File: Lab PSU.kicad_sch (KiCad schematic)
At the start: 2 parts, among them T1 Transformer_1P_SS, T2 Transformer_1P_SS

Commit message: many changes
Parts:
- removed T1, T2: Transformer_1P_SS, symbol Device:Transformer_1P_SS
- added C1, C2, C3, C4: 2200u, Capacitor_THT:CP_Radial_D18.0mm_P7.50mm, symbol Device:C_Polarized
- added C27, C28, C35: 10u, Capacitor_THT:CP_Radial_D18.0mm_P7.50mm, symbol Device:C_Polarized
- added C29, C33, C34: 220u, Capacitor_THT:CP_Radial_D18.0mm_P7.50mm, symbol Device:C_Polarized
- added C31, C32, C37: 22u, Capacitor_THT:CP_Radial_D18.0mm_P7.50mm, symbol Device:C_Polarized
- added C36, C38, C39: 100n, Capacitor_SMD:C_1210_3225Metric_Pad1.33x2.70mm_HandSolder, symbol Device:C
- added D1, D10, D11, D12, D13, D14, D15, D16, D2, D24, D25, D26, D27, D28, D29, D3, D30, D31, D4, D5, D6, D7, D8, D9: 1N5406, Diode_THT:D_DO-201AD_P15.24mm_Horizontal, symbol Diode:1N5406
- added F1: 3A slow, symbol Device:Fuse
- added F2, F3: 1A slow, symbol Device:Fuse
- added J1: Screw_Terminal_01x04, TerminalBlock_4Ucon:TerminalBlock_4Ucon_1x04_P3.50mm_Vertical, symbol Connector:Screw_Terminal_01x04
- added J4, J5, J6, J7: Screw_Terminal_01x03, TerminalBlock_4Ucon:TerminalBlock_4Ucon_1x03_P3.50mm_Vertical, symbol Connector:Screw_Terminal_01x03
- added R47, R48, R55: 120, Resistor_SMD:R_1210_3225Metric_Pad1.30x2.65mm_HandSolder, symbol Device:R
- added R49, R50, R57: 330, Resistor_SMD:R_1210_3225Metric_Pad1.30x2.65mm_HandSolder, symbol Device:R
- added RV2, RV3, RV8: 2.5k, Potentiometer_THT:Potentiometer_Bourns_3299W_Vertical, symbol Device:R_Potentiometer_Trim
- added SW3: SW_DPDT_x2, symbol Switch:SW_DPDT_x2
- added T1: PowerTran M5225C, symbol Device:Transformer_1P_2S
- added TR1, TR2: PowerTran M4318, Transformers:Transformer 53x53, symbol Transformer:TRANSF6
- added U14, U17: LM317_SOT-223, Package_TO_SOT_SMD:SOT-223-3_TabPin2, symbol Regulator_Linear:LM317_SOT-223
- added U15: LM337_SOT223, Package_TO_SOT_SMD:SOT-223-3_TabPin2, symbol Regulator_Linear:LM337_SOT223
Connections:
- net 230VAC: now also F1.1, F2.1, F3.1, SW3.3 (C)
- net GND: now also C1.2, C2.2, C29.2, C3.2, C35.2, C37.2, C39.1, C4.2, D1.2 (A), D13.2 (A), D14.2 (A), D15.2 (A), D16.2 (A), D2.2 (A), D26.2 (A), D27.2 (A), D28.1 (K), D28.2 (A), D3.2 (A), D4.2 (A), R57.1, RV8.2, RV8.3, TR2.5, TR2.7
- net NEUT: now also J6.2 (Pin_2), J7.2 (Pin_2), SW3.6 (C), T1.2 (AB), TR1.4, TR2.4
- new net: F2.2, J6.1 (Pin_1), TR1.1
- new net: TR1.2, TR1.3
- new net: F3.2, J7.1 (Pin_1), TR2.1
- new net: C34.2, D30.2 (A), D31.2 (A), U15.2 (VI)
- new net: F1.2, T1.1 (AA)
- new net: C27.2, R48.1, RV2.1, U15.1 (ADJ)
- new net: J1.4 (Pin_4), T1.4 (SB)
- new net: J1.1 (Pin_1), T1.5 (SC)
- new net: C35.1, R55.1, RV8.1, U17.1 (ADJ)
- new net: C28.1, R47.2, RV3.1, U14.1 (ADJ)
- new net: C33.1, D24.1 (K), D29.1 (K), U14.3 (VI)
- new net: C29.1, D25.1 (K), D27.1 (K), U17.3 (VI)
- new net: TR2.2, TR2.3
- new net +25VAC: D1.1 (K), D2.1 (K), D3.1 (K), D4.1 (K), D5.2 (A), D6.2 (A), D7.2 (A), D8.2 (A), J1.2 (Pin_2), T1.3 (SA)
- new net +35VDC: C1.1, C2.1, C3.1, C4.1, D10.1 (K), D11.1 (K), D12.1 (K), D5.1 (K), D6.1 (K), D7.1 (K), D8.1 (K), D9.1 (K)
- new net +5V: C37.1, C39.2, R55.2, R57.2, U17.2 (VO)
- new net +9VAC: D25.2 (A), D26.1 (K), TR2.6, TR2.8
- new net 0VAC: D10.2 (A), D11.2 (A), D12.2 (A), D13.1 (K), D14.1 (K), D15.1 (K), D16.1 (K), D9.2 (A), J1.3 (Pin_3), T1.6 (SD)
- new net Earth: J6.3 (Pin_3), J7.3 (Pin_3)
- new net MAINS IN: SW3.2 (B)
- new net NEUT IN: SW3.5 (B)
- new net V_{OUT}: C27.1, C28.2, C31.1, C32.2, C33.2, C34.1, C36.1, C38.2, R49.2, R50.1, RV2.2, RV2.3, RV3.2, RV3.3, TR1.6, TR1.7
- new net V_{OUT}+5V: C32.1, C36.2, R47.1, R50.2, U14.2 (VO)
- new net V_{OUT}+9VAC: D24.2 (A), D30.1 (K), TR1.8
- new net V_{OUT}-5V: C31.2, C38.1, R48.2, R49.1, U15.3 (VO)
- new net V_{OUT}-9VAC: D29.2 (A), D31.1 (K), TR1.5
- no-connect marks 0 -> 2
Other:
- sheet FrontPanel ports: added CC_{thermal}, CV_{thermal}, OE, SCL0, SDA0; removed none
- sheet HMI ports: added CC_{thermal}, CV_{thermal}, OE, SCL0, SDA0; removed none
- note added: "FrontPanel contains the linear regulator and feedback path. It sits on the back of the front panel."
- note added: "HMI contains the front side of the front panel, the Human Machine Interface, presenting controls and status to the user."

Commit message: do some work on the regulator boards
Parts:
- removed J5: Screw_Terminal_01x03, TerminalBlock_4Ucon:TerminalBlock_4Ucon_1x03_P3.50mm_Vertical, symbol Connector:Screw_Terminal_01x03
- added J8: Screw_Terminal_01x02, TerminalBlock_4Ucon:TerminalBlock_4Ucon_1x02_P3.50mm_Horizontal, symbol Connector:Screw_Terminal_01x02
- C27, C28, C35: footprint Capacitor_THT:CP_Radial_D18.0mm_P7.50mm -> Capacitor_THT:CP_Radial_D5.0mm_P2.00mm
- C29, C33, C34: footprint Capacitor_THT:CP_Radial_D18.0mm_P7.50mm -> Capacitor_THT:CP_Radial_D10.0mm_P5.00mm_P7.50mm
- C31, C32, C37: footprint Capacitor_THT:CP_Radial_D18.0mm_P7.50mm -> Capacitor_THT:CP_Radial_D6.3mm_P2.50mm
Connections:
- net +5V: now also J8.1 (Pin_1)
- net GND: now also J8.2 (Pin_2)
- net V_{OUT}: now also C38.1, J4.2 (Pin_2); no longer C38.2
- net V_{OUT}+5V: now also J4.1 (Pin_1)
- net V_{OUT}-5V: now also C38.2, J4.3 (Pin_3); no longer C38.1
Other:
- moved on the sheet: C38

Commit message: shrink regulator board a little
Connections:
- net V_{OUT}+5V: now also J4.3 (Pin_3); no longer J4.1 (Pin_1)
- net V_{OUT}-5V: now also J4.1 (Pin_1); no longer J4.3 (Pin_3)
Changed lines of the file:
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@@
 		(lib_id "Connector:Screw_Terminal_01x03")
 		(at 182.88 91.44 0)
+		(mirror x)
 		(unit 1)
 		(exclude_from_sim no)
@@
 		(dnp no)
 		(property "Reference" "J4"
-			(at 182.88 82.55 0)
+			(at 182.88 100.33 0)
 			(effects
 				(font
@@
 		)
 		(property "Value" "Screw_Terminal_01x03"
-			(at 182.88 85.09 0)
+			(at 182.88 97.79 0)
 			(effects
 				(font

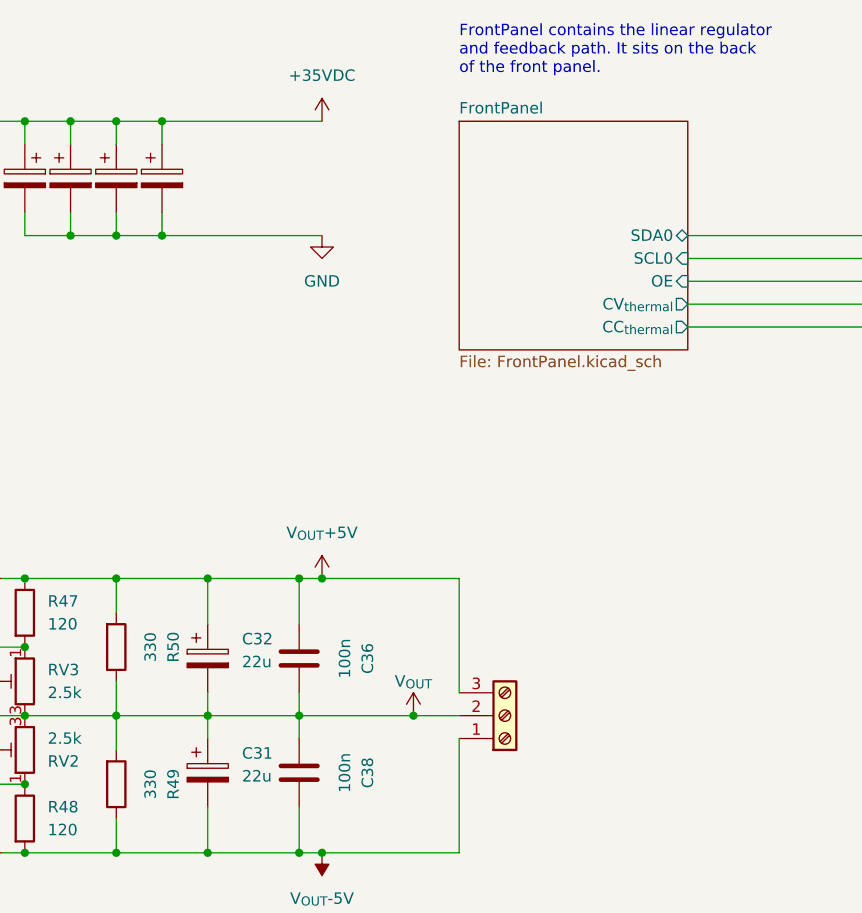
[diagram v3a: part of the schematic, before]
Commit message: kicad v10. many changes to invididual boards
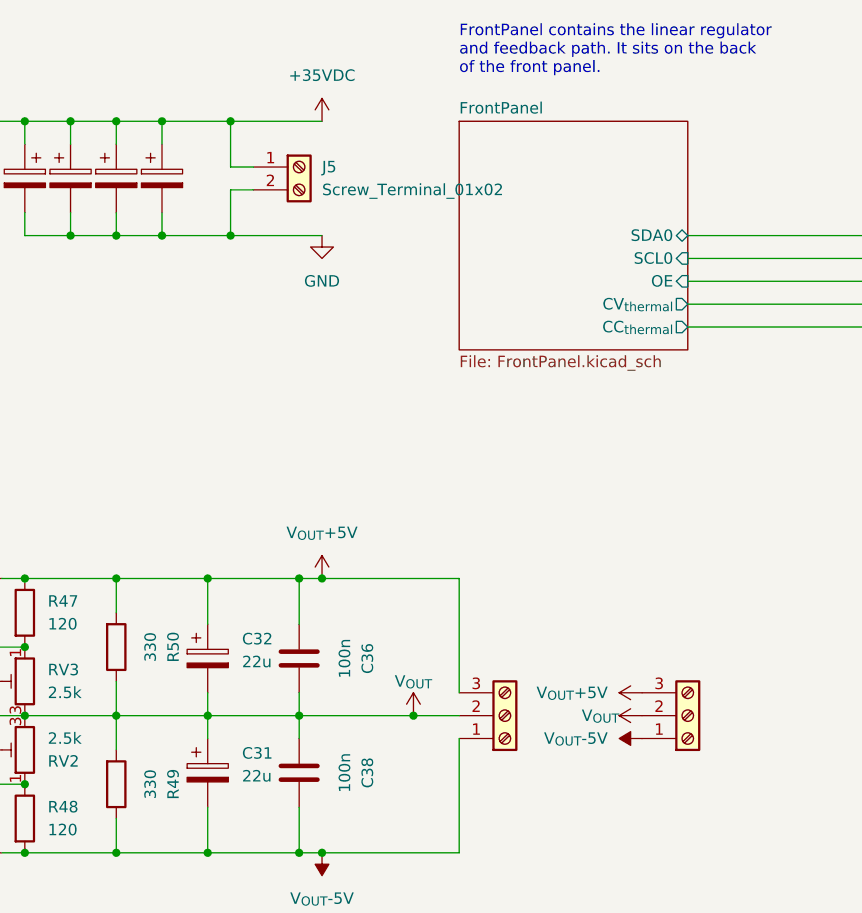
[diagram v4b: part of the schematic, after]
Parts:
- added J11: Screw_Terminal_01x03, TerminalBlock_4Ucon:TerminalBlock_4Ucon_1x03_P3.50mm_Vertical, symbol Connector:Screw_Terminal_01x03
- added J5: Screw_Terminal_01x02, TerminalBlock_4Ucon:TerminalBlock_4Ucon_1x02_P3.50mm_Horizontal, symbol Connector:Screw_Terminal_01x02
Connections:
- net +35VDC: now also J5.1 (Pin_1)
- net GND: now also J5.2 (Pin_2)
- net V_{OUT}: now also J11.2 (Pin_2)
- net V_{OUT}+5V: now also J11.3 (Pin_3)
- net V_{OUT}-5V: now also J11.1 (Pin_1)

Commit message: interim commit
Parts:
- added J12, J13, J14, J15, J16, J17, J18: Conn_01x20, Connector_PinSocket_2.54mm:PinSocket_1x20_P2.54mm_Vertical, symbol Connector_Generic:Conn_01x20
- added J19, J20: Conn_01x20, Connector_PinHeader_2.54mm:PinHeader_1x20_P2.54mm_Vertical, symbol Connector_Generic:Conn_01x20
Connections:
- net +35VDC: now also J17.1 (Pin_1), J17.10 (Pin_10), J17.11 (Pin_11), J17.12 (Pin_12), J17.13 (Pin_13), J17.14 (Pin_14), J17.15 (Pin_15), J17.16 (Pin_16), J17.17 (Pin_17), J17.18 (Pin_18), J17.19 (Pin_19), J17.2 (Pin_2), J17.20 (Pin_20), J17.3 (Pin_3), J17.4 (Pin_4), J17.5 (Pin_5), J17.6 (Pin_6), J17.7 (Pin_7), J17.8 (Pin_8), J17.9 (Pin_9), J19.1 (Pin_1), J19.10 (Pin_10), J19.11 (Pin_11), J19.12 (Pin_12), J19.13 (Pin_13), J19.14 (Pin_14), J19.15 (Pin_15), J19.16 (Pin_16), J19.17 (Pin_17), J19.18 (Pin_18), J19.19 (Pin_19), J19.2 (Pin_2), J19.20 (Pin_20), J19.3 (Pin_3), J19.4 (Pin_4), J19.5 (Pin_5), J19.6 (Pin_6), J19.7 (Pin_7), J19.8 (Pin_8), J19.9 (Pin_9)
- net +5V: now also J15.1 (Pin_1), J15.10 (Pin_10), J15.11 (Pin_11), J15.12 (Pin_12), J15.13 (Pin_13), J15.14 (Pin_14), J15.15 (Pin_15), J15.16 (Pin_16), J15.17 (Pin_17), J15.18 (Pin_18), J15.19 (Pin_19), J15.2 (Pin_2), J15.20 (Pin_20), J15.3 (Pin_3), J15.4 (Pin_4), J15.5 (Pin_5), J15.6 (Pin_6), J15.7 (Pin_7), J15.8 (Pin_8), J15.9 (Pin_9)
- net GND: now also J16.1 (Pin_1), J16.10 (Pin_10), J16.11 (Pin_11), J16.12 (Pin_12), J16.13 (Pin_13), J16.14 (Pin_14), J16.15 (Pin_15), J16.16 (Pin_16), J16.17 (Pin_17), J16.18 (Pin_18), J16.19 (Pin_19), J16.2 (Pin_2), J16.20 (Pin_20), J16.3 (Pin_3), J16.4 (Pin_4), J16.5 (Pin_5), J16.6 (Pin_6), J16.7 (Pin_7), J16.8 (Pin_8), J16.9 (Pin_9), J18.1 (Pin_1), J18.10 (Pin_10), J18.11 (Pin_11), J18.12 (Pin_12), J18.13 (Pin_13), J18.14 (Pin_14), J18.15 (Pin_15), J18.16 (Pin_16), J18.17 (Pin_17), J18.18 (Pin_18), J18.19 (Pin_19), J18.2 (Pin_2), J18.20 (Pin_20), J18.3 (Pin_3), J18.4 (Pin_4), J18.5 (Pin_5), J18.6 (Pin_6), J18.7 (Pin_7), J18.8 (Pin_8), J18.9 (Pin_9), J20.1 (Pin_1), J20.10 (Pin_10), J20.11 (Pin_11), J20.12 (Pin_12), J20.13 (Pin_13), J20.14 (Pin_14), J20.15 (Pin_15), J20.16 (Pin_16), J20.17 (Pin_17), J20.18 (Pin_18), J20.19 (Pin_19), J20.2 (Pin_2), J20.20 (Pin_20), J20.3 (Pin_3), J20.4 (Pin_4), J20.5 (Pin_5), J20.6 (Pin_6), J20.7 (Pin_7), J20.8 (Pin_8), J20.9 (Pin_9); no longer D27.2 (A), D28.1 (K), TR2.5, TR2.7
- net V_{OUT}: now also J13.1 (Pin_1), J13.10 (Pin_10), J13.11 (Pin_11), J13.12 (Pin_12), J13.13 (Pin_13), J13.14 (Pin_14), J13.15 (Pin_15), J13.16 (Pin_16), J13.17 (Pin_17), J13.18 (Pin_18), J13.19 (Pin_19), J13.2 (Pin_2), J13.20 (Pin_20), J13.3 (Pin_3), J13.4 (Pin_4), J13.5 (Pin_5), J13.6 (Pin_6), J13.7 (Pin_7), J13.8 (Pin_8), J13.9 (Pin_9); no longer J4.2 (Pin_2)
- net V_{OUT}+5V: now also J12.1 (Pin_1), J12.10 (Pin_10), J12.11 (Pin_11), J12.12 (Pin_12), J12.13 (Pin_13), J12.14 (Pin_14), J12.15 (Pin_15), J12.16 (Pin_16), J12.17 (Pin_17), J12.18 (Pin_18), J12.19 (Pin_19), J12.2 (Pin_2), J12.20 (Pin_20), J12.3 (Pin_3), J12.4 (Pin_4), J12.5 (Pin_5), J12.6 (Pin_6), J12.7 (Pin_7), J12.8 (Pin_8), J12.9 (Pin_9); no longer J4.3 (Pin_3)
- net V_{OUT}-5V: now also J14.1 (Pin_1), J14.10 (Pin_10), J14.11 (Pin_11), J14.12 (Pin_12), J14.13 (Pin_13), J14.14 (Pin_14), J14.15 (Pin_15), J14.16 (Pin_16), J14.17 (Pin_17), J14.18 (Pin_18), J14.19 (Pin_19), J14.2 (Pin_2), J14.20 (Pin_20), J14.3 (Pin_3), J14.4 (Pin_4), J14.5 (Pin_5), J14.6 (Pin_6), J14.7 (Pin_7), J14.8 (Pin_8), J14.9 (Pin_9); no longer J4.1 (Pin_1)
- new net: D27.2 (A), D28.1 (K), TR2.5, TR2.7
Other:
- moved on the sheet: J8
